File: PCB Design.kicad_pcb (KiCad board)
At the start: 2 copper layers, 17 parts, among them J1 Serial, J2 Digital Pins, J3 I2C, J4 ICSP, U1 24LC1025, U2 24LC1025, U3 DS1337, U4 ATMEGA328P-AU, Y1 Crystal 32MHz, Y2 Crystal 16MHz

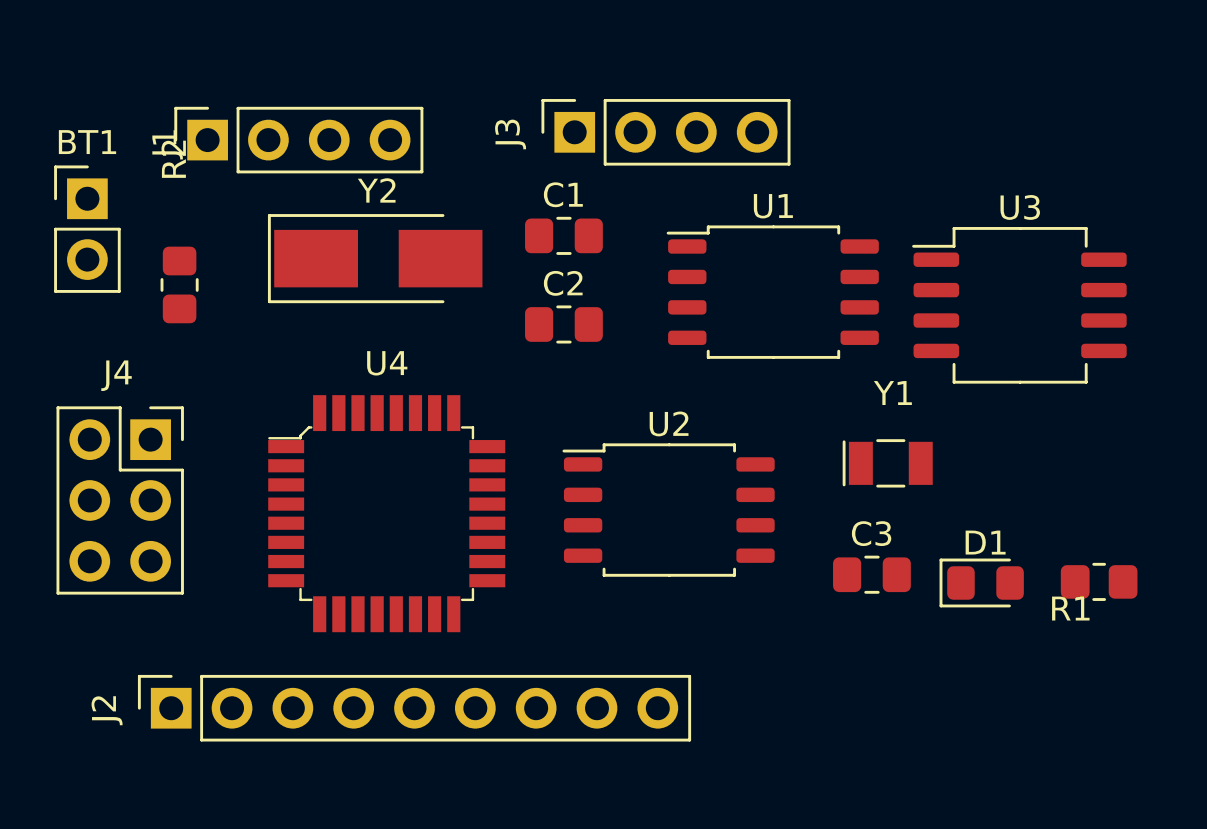
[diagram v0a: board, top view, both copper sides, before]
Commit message: add outline and mounting holes
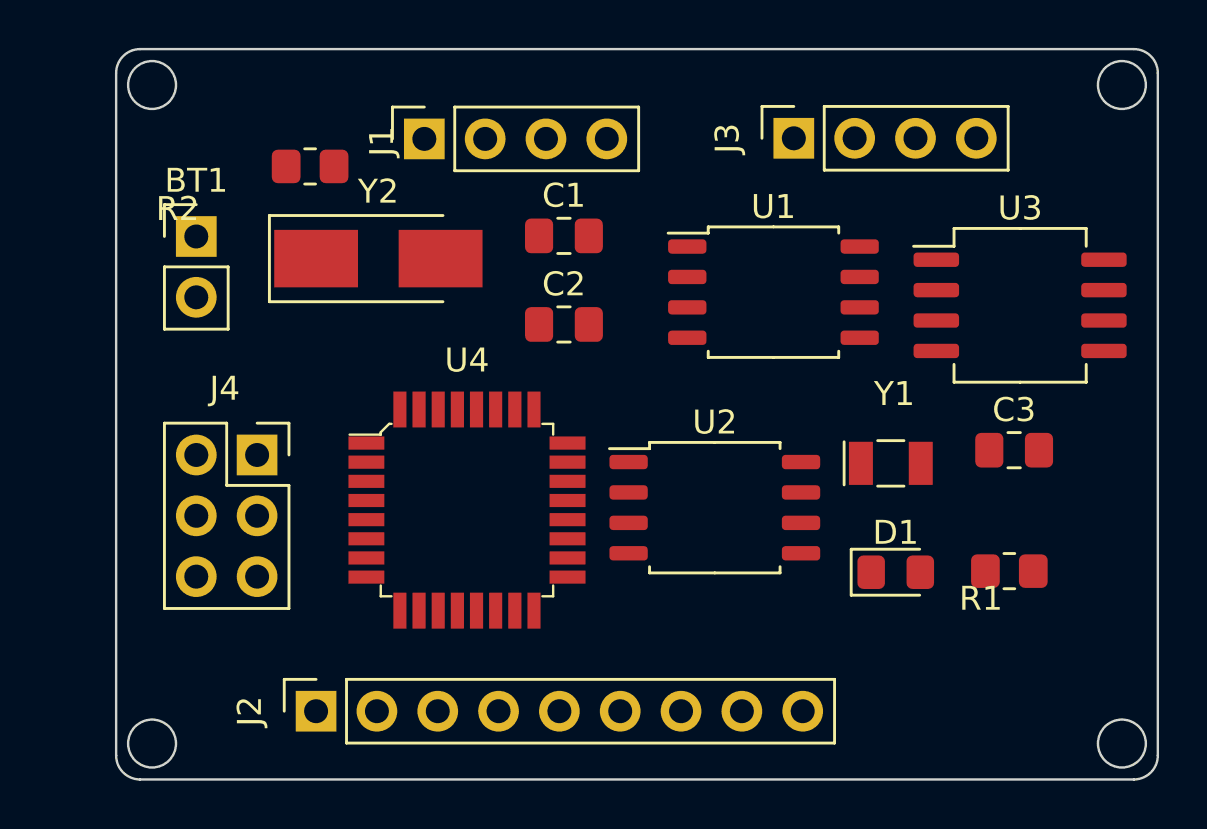
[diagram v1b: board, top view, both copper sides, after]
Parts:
- moved J3 9.15 mm to (98.8, 103.7)
- moved J1 9.05 mm to (83.4, 103.8)
- moved C3 7.89 mm to (108.0, 116.8)
- moved R2 7.36 mm to (78.6, 104.9), turned to 180 degrees
- moved J2 6.05 mm to (78.8, 127.7)
- moved BT1 4.81 mm to (73.8, 107.8)
- moved J4 4.49 mm to (76.4, 117.0)
- moved D1 3.78 mm to (103.1, 121.8)
- moved R1 3.78 mm to (107.8, 121.8)
- moved U4 3.35 mm to (85.2, 119.2)
- moved U2 1.90 mm to (95.5, 119.2)
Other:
- board outline added: 43.5 x 30.5 mm
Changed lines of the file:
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@@
   (net 31 "unconnected-(U4-Pad26)")
   (footprint "Connector_PinSocket_2.54mm:PinSocket_1x04_P2.54mm_Vertical" (layer "F.Cu")
-    (at 74.32 103.8 90)
+    (at 83.37 103.75 90)
     (descr "Through hole straight socket strip, 1x04, 2.54mm pitch, single row (from Kicad 4.0.7), script generated")
     (tags "Through hole socket strip THT 1x04 2.54mm single row")
@@
   )
   (footprint "Package_SO:SOIC-8_5.23x5.23mm_P1.27mm" (layer "F.Cu")
-    (at 93.6 119.25)
+    (at 95.5 119.15)
     (descr "SOIC, 8 Pin (http://www.winbond.com/resource-files/w25q32jv%20revg%2003272018%20plus.pdf#page=68), generated with kicad-footprint-generator ipc_gullwing_generator.py")
     (tags "SOIC SO")
@@
   )
   (footprint "Connector_PinSocket_2.54mm:PinSocket_2x03_P2.54mm_Vertical" (layer "F.Cu")
-    (at 71.94 116.31)
+    (at 76.386905 116.95)
     (descr "Through hole straight socket strip, 2x03, 2.54mm pitch, double cols (from Kicad 4.0.7), script generated")
     (tags "Through hole socket strip THT 2x03 2.54mm double row")
@@
   )
   (footprint "LED_SMD:LED_0805_2012Metric_Pad1.15x1.40mm_HandSolder" (layer "F.Cu")
-    (at 106.805 122.295)
+    (at 103.055 121.845)
     (descr "LED SMD 0805 (2012 Metric), square (rectangular) end terminal, IPC_7351 nominal, (Body size source: https://docs.google.com/spreadsheets/d/1BsfQQcO9C6DZCsRaXUlFlo91Tg2WpOkGARC1WS5S8t0/edit?usp=sharing), generated with kicad-footprint-generator")
     (tags "LED handsolder")
@@
   )
   (footprint "Connector_PinHeader_2.54mm:PinHeader_1x02_P2.54mm_Vertical" (layer "F.Cu")
-    (at 69.3 106.25)
+    (at 73.846905 107.825)
     (descr "Through hole straight pin header, 1x02, 2.54mm pitch, single row")
     (tags "Through hole pin header THT 1x02 2.54mm single row")
@@
       (effects (font (size 1 1) (thickness 0.15)))
     )
-    (fp_text value "Battery 3V" (at 0 4.87) (layer "F.Fab")
+    (fp_text value "Battery 3V" (at 0.653095 5.175) (layer "F.Fab")
       (effects (font (size 1 1) (thickness 0.15)))
     )
@@
   )
   (footprint "Capacitor_SMD:C_0805_2012Metric_Pad1.18x1.45mm_HandSolder" (layer "F.Cu")
-    (at 102.0625 121.95)
+    (at 108 116.75)
     (descr "Capacitor SMD 0805 (2012 Metric), square (rectangular) end terminal, IPC_7351 nominal with elongated pad for handsoldering. (Body size source: IPC-SM-782 page 76, https://www.pcb-3d.com/wordpress/wp-content/uploads/ipc-sm-782a_amendment_1_and_2.pdf, https://docs.google.com/spreadsheets/d/1BsfQQcO9C6DZCsRaXUlFlo91Tg2WpOkGARC1WS5S8t0/edit?usp=sharing), generated with kicad-footprint-generator")
     (tags "capacitor handsolder")
@@
   )
   (footprint "Connector_PinSocket_2.54mm:PinSocket_1x09_P2.54mm_Vertical" (layer "F.Cu")
-    (at 72.8 127.525 90)
+    (at 78.85 127.65 90)
     (descr "Through hole straight socket strip, 1x09, 2.54mm pitch, single row (from Kicad 4.0.7), script generated")
     (tags "Through hole socket strip THT 1x09 2.54mm single row")
@@
       (effects (font (size 1 1) (thickness 0.15)))
     )
-    (fp_text value "Digital Pins" (at 0 23.09 90) (layer "F.Fab")
+    (fp_text value "Digital Pins" (at 1.3 22.7 90) (layer "F.Fab")
       (effects (font (size 1 1) (thickness 0.15)))
     )
@@
   )
   (footprint "Resistor_SMD:R_0805_2012Metric_Pad1.20x1.40mm_HandSolder" (layer "F.Cu")
-    (at 73.15 109.85 90)
+    (at 78.6 104.9 180)
     (descr "Resistor SMD 0805 (2012 Metric), square (rectangular) end terminal, IPC_7351 nominal with elongated pad for handsoldering. (Body size source: IPC-SM-782 page 72, https://www.pcb-3d.com/wordpress/wp-content/uploads/ipc-sm-782a_amendment_1_and_2.pdf), generated with kicad-footprint-generator")
     (tags "resistor handsolder")
@@
     (property "Sheetname" "")
     (attr smd)
-    (fp_text reference "R2" (at 5.25 -0.2 90) (layer "F.SilkS")
-      (effects (font (size 1 1) (thickness 0.15)))
-    )
-    (fp_text value "10KOhm" (at 0 1.65 90) (layer "F.Fab")
-      (effects (font (size 1 1) (thickness 0.15)))
-    )
-    (fp_text user "${REFERENCE}" (at 0 0 90) (layer "F.Fab")
+    (fp_text reference "R2" (at 5.526905 -1.775) (layer "F.SilkS")
+      (effects (font (size 1 1) (thickness 0.15)))
+    )
+    (fp_text value "10KOhm" (at 0 1.65) (layer "F.Fab")
+      (effects (font (size 1 1) (thickness 0.15)))
+    )
+    (fp_text user "${REFERENCE}" (at 6.05 -0.5) (layer "F.Fab")
       (effects (font (size 0.5 0.5) (thickness 0.08)))
     )
@@
     (fp_line (start 1 -0.625) (end 1 0.625) (layer "F.Fab") (width 0.1))
     (fp_line (start -1 0.625) (end -1 -0.625) (layer "F.Fab") (width 0.1))
-    (pad "1" smd roundrect (at -1 0 90) (size 1.2 1.4) (layers "F.Cu" "F.Paste" "F.Mask") (roundrect_rratio 0.208333)
+    (pad "1" smd roundrect (at -1 0 180) (size 1.2 1.4) (layers "F.Cu" "F.Paste" "F.Mask") (roundrect_rratio 0.208333)
       (net 20 "/RESET") (pintype "passive"))
-    (pad "2" smd roundrect (at 1 0 90) (size 1.2 1.4) (layers "F.Cu" "F.Paste" "F.Mask") (roundrect_rratio 0.208333)
+    (pad "2" smd roundrect (at 1 0 180) (size 1.2 1.4) (layers "F.Cu" "F.Paste" "F.Mask") (roundrect_rratio 0.208333)
       (net 1 "/Vcc") (pintype "passive"))
     (model "${KICAD6_3DMODEL_DIR}/Resistor_SMD.3dshapes/R_0805_2012Metric.wrl"
@@
   )
   (footprint "Connector_PinSocket_2.54mm:PinSocket_1x04_P2.54mm_Vertical" (layer "F.Cu")
-    (at 89.65 103.475 90)
+    (at 98.8 103.725 90)
     (descr "Through hole straight socket strip, 1x04, 2.54mm pitch, single row (from Kicad 4.0.7), script generated")
     (tags "Through hole socket strip THT 1x04 2.54mm single row")
@@
   )
   (footprint "digikey-footprints:TQFP-32_7x7mm" (layer "F.Cu")
-    (at 81.8 119.4)
+    (at 85.15 119.25)
     (descr "http://www.atmel.com/Images/Atmel-8826-SEEPROM-PCB-Mounting-Guidelines-Surface-Mount-Packages-ApplicationNote.pdf")
     (property "Category" "Integrated Circuits (ICs)")
@@
       (effects (font (size 1 1) (thickness 0.15)))
     )
-    (fp_text value "ATMEGA328P-AU" (at -2.11 7.925) (layer "F.Fab")
+    (fp_text value "ATMEGA328P-AU" (at 3.94 8.05) (layer "F.Fab")
       (effects (font (size 1 1) (thickness 0.15)))
     )
@@
   )
   (footprint "Resistor_SMD:R_0805_2012Metric_Pad1.20x1.40mm_HandSolder" (layer "F.Cu")
-    (at 111.55 122.25)
+    (at 107.8 121.8)
     (descr "Resistor SMD 0805 (2012 Metric), square (rectangular) end terminal, IPC_7351 nominal with elongated pad for handsoldering. (Body size source: IPC-SM-782 page 72, https://www.pcb-3d.com/wordpress/wp-content/uploads/ipc-sm-782a_amendment_1_and_2.pdf), generated with kicad-footprint-generator")
     (tags "resistor handsolder")
@@
     )
   )
+  (gr_line (start 114 101) (end 114 129.5) (layer "Edge.Cuts") (width 0.1))
+  (gr_circle (center 72 101.5) (end 73 101.5) (layer "Edge.Cuts") (width 0.1) (fill none))
+  (gr_line (start 70.5 101) (end 70.5 129.5) (layer "Edge.Cuts") (width 0.1))
+  (gr_line (start 71.5 100) (end 113 100) (layer "Edge.Cuts") (width 0.1))
+  (gr_circle (center 112.5 129) (end 113.5 129) (layer "Edge.Cuts") (width 0.1) (fill none))
+  (gr_circle (center 112.5 101.5) (end 113.5 101.5) (layer "Edge.Cuts") (width 0.1) (fill none))
+  (gr_arc (start 70.5 101) (mid 70.792893 100.292893) (end 71.5 100) (layer "Edge.Cuts") (width 0.1))
+  (gr_arc (start 71.5 130.5) (mid 70.792893 130.207107) (end 70.5 129.5) (layer "Edge.Cuts") (width 0.1))
+  (gr_circle (center 72 129) (end 73 129) (layer "Edge.Cuts") (width 0.1) (fill none))
+  (gr_line (start 71.5 130.5) (end 113 130.5) (layer "Edge.Cuts") (width 0.1))
+  (gr_arc (start 114 129.5) (mid 113.707107 130.207107) (end 113 130.5) (layer "Edge.Cuts") (width 0.1))
+  (gr_arc (start 113 100) (mid 113.707107 100.292893) (end 114 101) (layer "Edge.Cuts") (width 0.1))
 )
